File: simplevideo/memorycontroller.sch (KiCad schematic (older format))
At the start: 13 parts, among them U19 74LS00, U2 74LS08, U20 74HC74, U21 74LS245, U22 74LS32, U23 74LS245, U24 74LS245, U25 74LS166, U26 62256, U28 74LS245, U29 74LS245, U9 74HC74

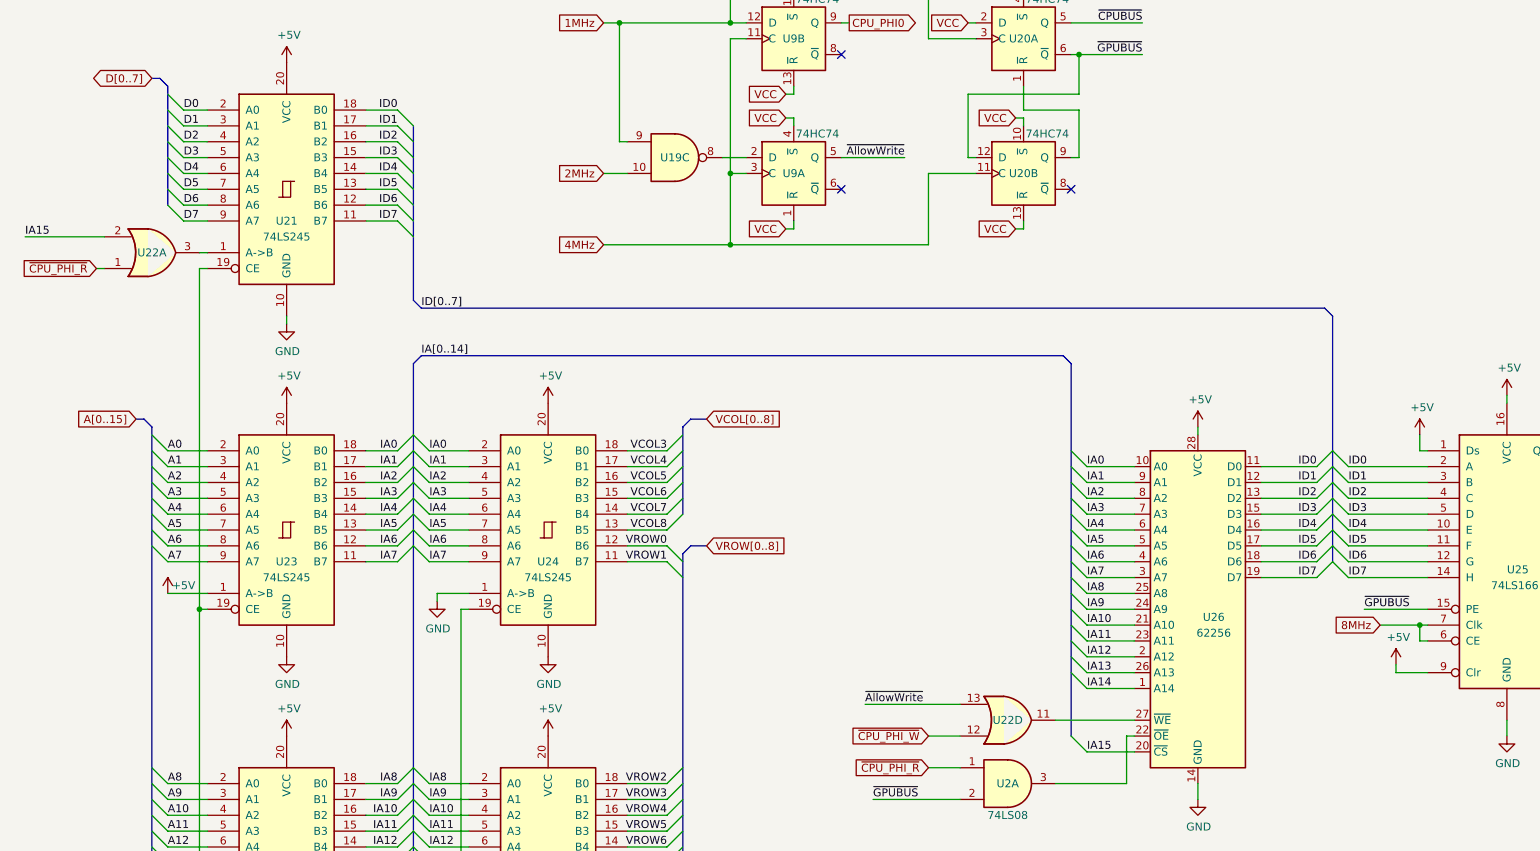
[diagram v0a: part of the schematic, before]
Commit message: New address decoding scheme and complete breadboard layout, should be ready to build
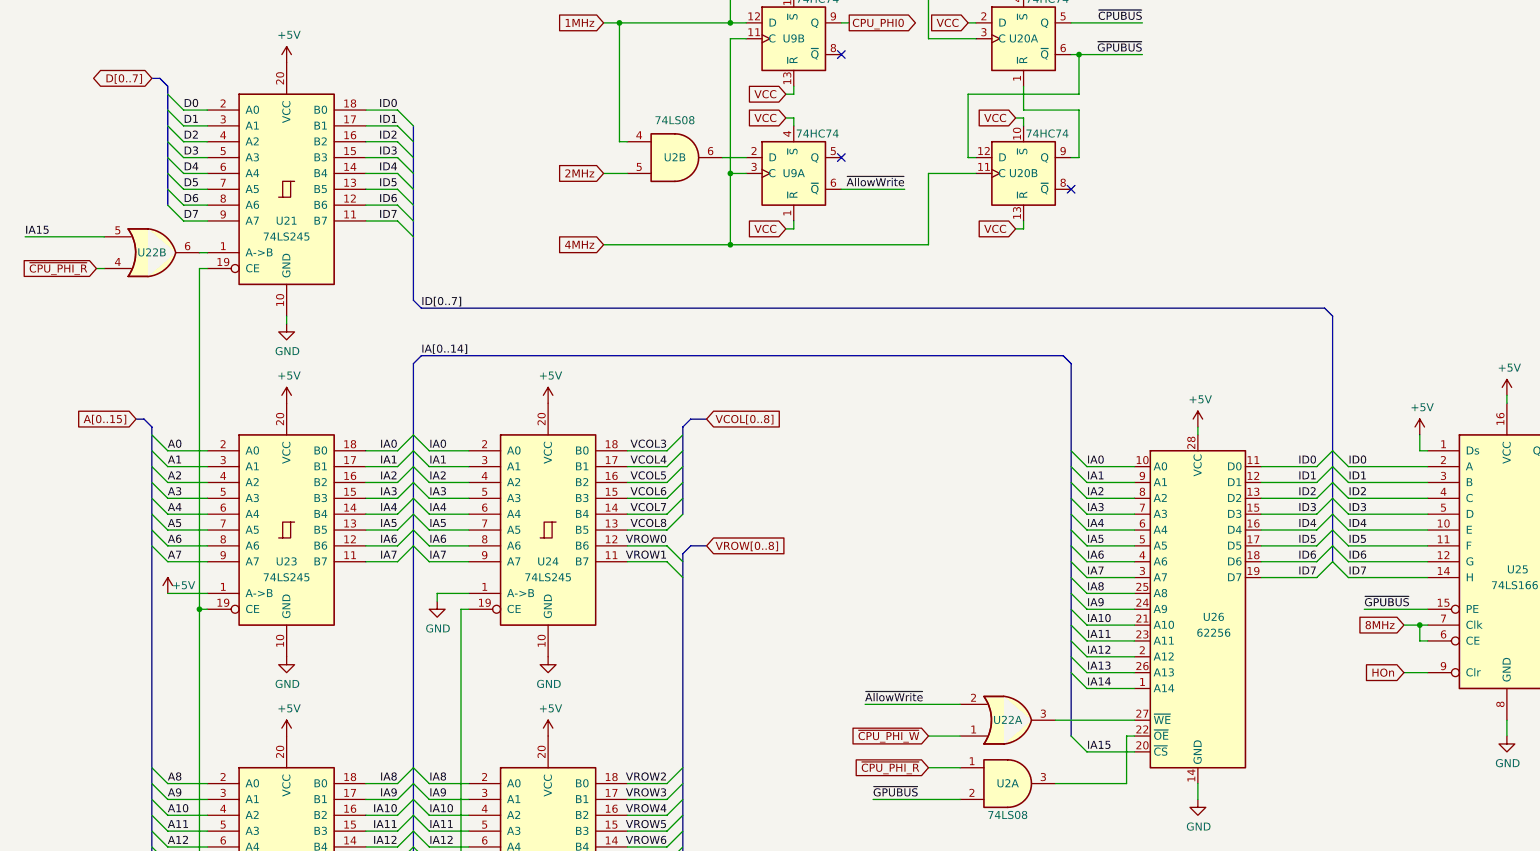
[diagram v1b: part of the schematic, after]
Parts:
- removed U19: 74LS00, Package_DIP:DIP-14_W7.62mm, symbol 74xx:74LS00
- added unit 2 of U2
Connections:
- net +5V: no longer U25.9 (Clr)
- net 1MHz: now also U2.4
- net 2MHz: now also U2.5
- net IA15: now also U22.5; no longer U22.2
- net ~AllowWrite: now also U22.2, U9.6 (~Q); no longer U22.13, U9.5 (Q)
- net ~CPU_PHI_R: now also U22.4; no longer U22.1
- net ~CPU_PHI_W: now also U22.1; no longer U22.12
- net at U21.1 (A->B): now also U22.6; no longer U22.3
- net at U26.27 (~WE): now also U22.3; no longer U22.11
- net at U9.2 (D): now also U2.6
- new net HOn: U25.9 (Clr)
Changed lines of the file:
@@
 $EndComp
 Wire Wire Line
-	9300 4900 9550 4900
+	9450 4900 9550 4900
 Wire Wire Line
 	9200 4800 9600 4800
@@
 $Comp
 L power:+5V #PWR?
-U 1 1 5EE8A196
-P 9400 5150
-AR Path="/5EE8A196" Ref="#PWR?"  Part="1"
-AR Path="/78D322BF/5EE8A196" Ref="#PWR?"  Part="1"
-AR Path="/5EE02DBD/5EE8A196" Ref="#PWR015"  Part="1"
-F 0 "#PWR015" H 9400 5000 50  0001 C CNN
-F 1 "+5V" H 9415 5323 50  0000 C CNN
-F 2 "" H 9400 5150 50  0001 C CNN
-F 3 "" H 9400 5150 50  0001 C CNN
-	1    9400 5150
-	1    0    0    -1
-$EndComp
-$Comp
-L power:+5V #PWR?
 U 1 1 5EE8A1A0
 P 10100 3450
@@
 	1    0    0    -1
 $EndComp
-Wire Wire Line
-	9400 5200 9400 5150
-Wire Wire Line
-	9600 5200 9400 5200
 Wire Wire Line
 	9600 5000 9550 5000
@@
 Wire Wire Line
 	7700 5600 7750 5600
-$Comp
-L 74xx:74LS00 U19
-U 3 1 5EE8A213
-P 4850 1950
-F 0 "U19" H 4850 1950 50  0000 C CNN
-F 1 "74LS00" H 4850 2184 50  0001 C CNN
-F 2 "Package_DIP:DIP-14_W7.62mm" H 4850 1950 50  0001 C CNN
-F 3 "http://www.ti.com/lit/gpn/sn74ls00" H 4850 1950 50  0001 C CNN
-	3    4850 1950
-	1    0    0    -1
-$EndComp
 Entry Wire Line
 	1550 6500 1650 6600
@@
 $Comp
 L 74xx:74LS32 U22
-U 1 1 5EE8A22A
+U 2 1 5EE8A22A
 P 1550 2550
 F 0 "U22" H 1550 2550 50  0000 C CNN
@@
 F 2 "Package_DIP:DIP-14_W7.62mm" H 1550 2550 50  0001 C CNN
 F 3 "http://www.ti.com/lit/gpn/sn74LS32" H 1550 2550 50  0001 C CNN
-	1    1550 2550
+	2    1550 2550
 	1    0    0    1
 $EndComp
@@
 Wire Wire Line
 	4550 6600 4700 6600
-Text GLabel 9300 4900 0    50   Input ~ 0
-8MHz
 $Comp
 L 74xx:74HC74 U20
@@
 $Comp
 L 74xx:74LS32 U22
-U 4 1 5EE8A265
+U 1 1 5EE8A265
 P 6950 5500
 F 0 "U22" H 6950 5500 50  0000 C CNN
@@
 F 2 "Package_DIP:DIP-14_W7.62mm" H 6950 5500 50  0001 C CNN
 F 3 "http://www.ti.com/lit/gpn/sn74LS32" H 6950 5500 50  0001 C CNN
-	4    6950 5500
+	1    6950 5500
 	1    0    0    1
 $EndComp
@@
 Wire Wire Line
 	7700 5600 7700 5900
-$Comp
-L 74xx:74HC74 U9
-U 1 1 5EE8A274
-P 5600 2050
-F 0 "U9" H 5600 2050 50  0000 C CNN
-F 1 "74HC74" H 5750 2300 50  0000 C CNN
-F 2 "Package_DIP:DIP-14_W7.62mm" H 5600 2050 50  0001 C CNN
-F 3 "74xx/74hc_hct74.pdf" H 5600 2050 50  0001 C CNN
-	1    5600 2050
-	1    0    0    -1
-$EndComp
-$Comp
-L 74xx:74HC74 U9
-U 2 1 5EE8A27E
-P 5600 1200
-F 0 "U9" H 5600 1200 50  0000 C CNN
-F 1 "74HC74" H 5750 1450 50  0000 C CNN
-F 2 "Package_DIP:DIP-14_W7.62mm" H 5600 1200 50  0001 C CNN
-F 3 "74xx/74hc_hct74.pdf" H 5600 1200 50  0001 C CNN
-	2    5600 1200
-	1    0    0    -1
-$EndComp
 Wire Wire Line
 	5600 1500 5600 1550
@@
 Connection ~ 5200 1100
 Wire Wire Line
-	5900 1950 6300 1950
-Text Label 6300 1950 2    50   ~ 0
+	5900 2150 6300 2150
+Text Label 6300 2150 2    50   ~ 0
 ~AllowWrite
 Text Label 6050 5400 0    50   ~ 0
 ~AllowWrite
-NoConn ~ 5900 2150
 Wire Wire Line
 	5200 2500 4400 2500
@@
 Wire Wire Line
 	7250 5900 7700 5900
+Wire Wire Line
+	9450 5200 9600 5200
+Text GLabel 9450 5200 0    50   Input ~ 0
+HOn
+Text GLabel 9450 4900 0    50   Input ~ 0
+8MHz
+$Comp
+L 74xx:74LS08 U2
+U 2 1 5F245F61
+P 4850 1950
+F 0 "U2" H 4850 1950 50  0000 C CNN
+F 1 "74LS08" H 4850 2184 50  0000 C CNN
+F 2 "" H 4850 1950 50  0001 C CNN
+F 3 "http://www.ti.com/lit/gpn/sn74LS08" H 4850 1950 50  0001 C CNN
+	2    4850 1950
+	1    0    0    -1
+$EndComp
+NoConn ~ 5900 1950
 Wire Bus Line
 	4900 4450 4900 6400
@@
 Wire Bus Line
 	7350 3250 7350 5600
+$Comp
+L 74xx:74HC74 U9
+U 2 1 5EE8A27E
+P 5600 1200
+F 0 "U9" H 5600 1200 50  0000 C CNN
+F 1 "74HC74" H 5750 1450 50  0000 C CNN
+F 2 "Package_DIP:DIP-14_W7.62mm" H 5600 1200 50  0001 C CNN
+F 3 "74xx/74hc_hct74.pdf" H 5600 1200 50  0001 C CNN
+	2    5600 1200
+	1    0    0    -1
+$EndComp
+$Comp
+L 74xx:74HC74 U9
+U 1 1 5EE8A274
+P 5600 2050
+F 0 "U9" H 5600 2050 50  0000 C CNN
+F 1 "74HC74" H 5750 2300 50  0000 C CNN
+F 2 "Package_DIP:DIP-14_W7.62mm" H 5600 2050 50  0001 C CNN
+F 3 "74xx/74hc_hct74.pdf" H 5600 2050 50  0001 C CNN
+	1    5600 2050
+	1    0    0    -1
+$EndComp
 $EndSCHEMATC

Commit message: Minor edits
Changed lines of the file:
@@
 Wire Bus Line
 	4900 4450 4950 4400
-Text Label 13350 5600 2    50   ~ 0
-CLK_16
-Wire Notes Line width 20 style solid rgb(0, 200, 0)
-	16600 5550 16700 5550
-Wire Notes Line width 20 style solid rgb(0, 200, 0)
-	16800 5550 16900 5550
-Wire Notes Line width 20 style solid rgb(0, 200, 0)
-	17000 5550 17100 5550
-Wire Notes Line width 20 style solid rgb(0, 200, 0)
-	17200 5550 17300 5550
-Wire Notes Line width 20 style solid rgb(0, 200, 0)
-	17400 5550 17500 5550
-Wire Notes Line width 20 style solid rgb(0, 200, 0)
-	17600 5550 17700 5550
-Wire Notes Line width 20 style solid rgb(0, 200, 0)
-	17800 5550 17900 5550
-Wire Notes Line width 20 style solid rgb(0, 200, 0)
-	18000 5550 18100 5550
-Wire Notes Line width 20 style solid rgb(0, 200, 0)
-	18200 5550 18300 5550
-Wire Notes Line width 20 style solid rgb(0, 200, 0)
-	18400 5550 18500 5550
-Wire Notes Line width 20 style solid rgb(0, 200, 0)
-	18600 5550 18700 5550
-Wire Notes Line width 20 style solid rgb(0, 200, 0)
-	18800 5550 18900 5550
-Wire Notes Line width 20 style solid rgb(0, 200, 0)
-	15800 5550 15900 5550
-Wire Notes Line width 20 style solid rgb(0, 200, 0)
-	16000 5550 16100 5550
-Wire Notes Line width 20 style solid rgb(0, 200, 0)
-	16200 5550 16300 5550
-Wire Notes Line width 20 style solid rgb(0, 200, 0)
-	16400 5550 16500 5550
-Wire Notes Line width 20 style solid rgb(0, 200, 0)
-	15000 5550 15100 5550
-Wire Notes Line width 20 style solid rgb(0, 200, 0)
-	15200 5550 15300 5550
-Wire Notes Line width 20 style solid rgb(0, 200, 0)
-	15400 5550 15500 5550
-Wire Notes Line width 20 style solid rgb(0, 200, 0)
-	15600 5550 15700 5550
-Wire Notes Line width 20 style solid rgb(0, 200, 0)
-	14200 5550 14300 5550
-Wire Notes Line width 20 style solid rgb(0, 200, 0)
-	14400 5550 14500 5550
-Wire Notes Line width 20 style solid rgb(0, 200, 0)
-	14600 5550 14700 5550
-Wire Notes Line width 20 style solid rgb(0, 200, 0)
-	14800 5550 14900 5550
-Wire Notes Line width 20 style solid rgb(0, 200, 0)
-	13400 5550 13500 5550
-Wire Notes Line width 20 style solid rgb(0, 200, 0)
-	13600 5550 13700 5550
-Wire Notes Line width 20 style solid rgb(0, 200, 0)
-	13800 5550 13900 5550
-Wire Notes Line width 20 style solid rgb(0, 200, 0)
-	14000 5550 14100 5550
-Wire Notes Line width 20 style solid rgb(0, 200, 0)
-	19600 5550 19700 5550
-Wire Notes Line width 20 style solid rgb(0, 200, 0)
-	19000 5550 19100 5550
-Wire Notes Line width 20 style solid rgb(0, 200, 0)
-	19200 5550 19300 5550
-Wire Notes Line width 20 style solid rgb(0, 200, 0)
-	19400 5550 19500 5550
-Text Label 13350 5800 2    50   ~ 0
-CLK_4
-Wire Notes Line width 20 style solid rgb(0, 200, 0)
-	18200 5750 18600 5750
-Wire Notes Line width 20 style solid rgb(0, 200, 0)
-	15800 5750 16200 5750
-Wire Notes Line width 20 style solid rgb(0, 200, 0)
-	17400 5750 17800 5750
-Wire Notes Line width 20 style solid rgb(0, 200, 0)
-	15000 5750 15400 5750
-Wire Notes Line width 20 style solid rgb(0, 200, 0)
-	16600 5750 17000 5750
-Wire Notes Line width 20 style solid rgb(0, 200, 0)
-	14200 5750 14600 5750
-Wire Notes Line width 20 style solid rgb(0, 200, 0)
-	13400 5750 13800 5750
-Wire Notes Line width 20 style solid rgb(0, 200, 0)
-	19000 5750 19400 5750
 Text GLabel 4400 1100 0    50   Input ~ 0
 1MHz
@@
 $EndComp
 NoConn ~ 5900 1950
-Wire Bus Line
-	4900 4450 4900 6400
-Wire Bus Line
-	4900 3650 4900 4200
-Wire Bus Line
-	1650 1500 1650 2250
-Wire Bus Line
-	3200 1750 3200 2850
-Wire Bus Line
-	9000 2950 9000 4500
-Wire Bus Line
-	1550 3650 1550 6500
-Wire Bus Line
-	3200 3250 3200 6500
-Wire Bus Line
-	7350 3250 7350 5600
 $Comp
 L 74xx:74HC74 U9
@@
 	1    0    0    -1
 $EndComp
+Wire Bus Line
+	4900 4450 4900 6400
+Wire Bus Line
+	4900 3650 4900 4200
+Wire Bus Line
+	1650 1500 1650 2250
+Wire Bus Line
+	3200 1750 3200 2850
+Wire Bus Line
+	9000 2950 9000 4500
+Wire Bus Line
+	1550 3650 1550 6500
+Wire Bus Line
+	3200 3250 3200 6500
+Wire Bus Line
+	7350 3250 7350 5600
 $EndSCHEMATC

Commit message: Fixed various issues discovered during building and testing
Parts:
- U2: footprint (none) -> Package_DIP:DIP-14_W7.62mm
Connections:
- net 2MHz renamed ~2MHz
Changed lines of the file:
@@
 1MHz
 Text GLabel 4400 2050 0    50   Input ~ 0
-2MHz
+~2MHz
 Text GLabel 4400 2500 0    50   Input ~ 0
 4MHz
@@
 F 0 "U2" H 4850 1950 50  0000 C CNN
 F 1 "74LS08" H 4850 2184 50  0000 C CNN
-F 2 "" H 4850 1950 50  0001 C CNN
+F 2 "Package_DIP:DIP-14_W7.62mm" H 4850 1950 50  0001 C CNN
 F 3 "http://www.ti.com/lit/gpn/sn74LS08" H 4850 1950 50  0001 C CNN
 	2    4850 1950
